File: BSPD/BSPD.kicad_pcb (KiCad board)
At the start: 2 copper layers, 76 x 56 mm, 32 parts, among them Q3 PMOS, U1 LM339DR, U10 641964-1, U2 SN74LVC1G08DBVR, U3 NE555DR, U4 SN74LVC3G14DCUR, U5 SN74AC32DR, U6 SN74LVC1G08DBVR, U7 641964-1, U8 R-78E5.0-0.5, U9 641964-1

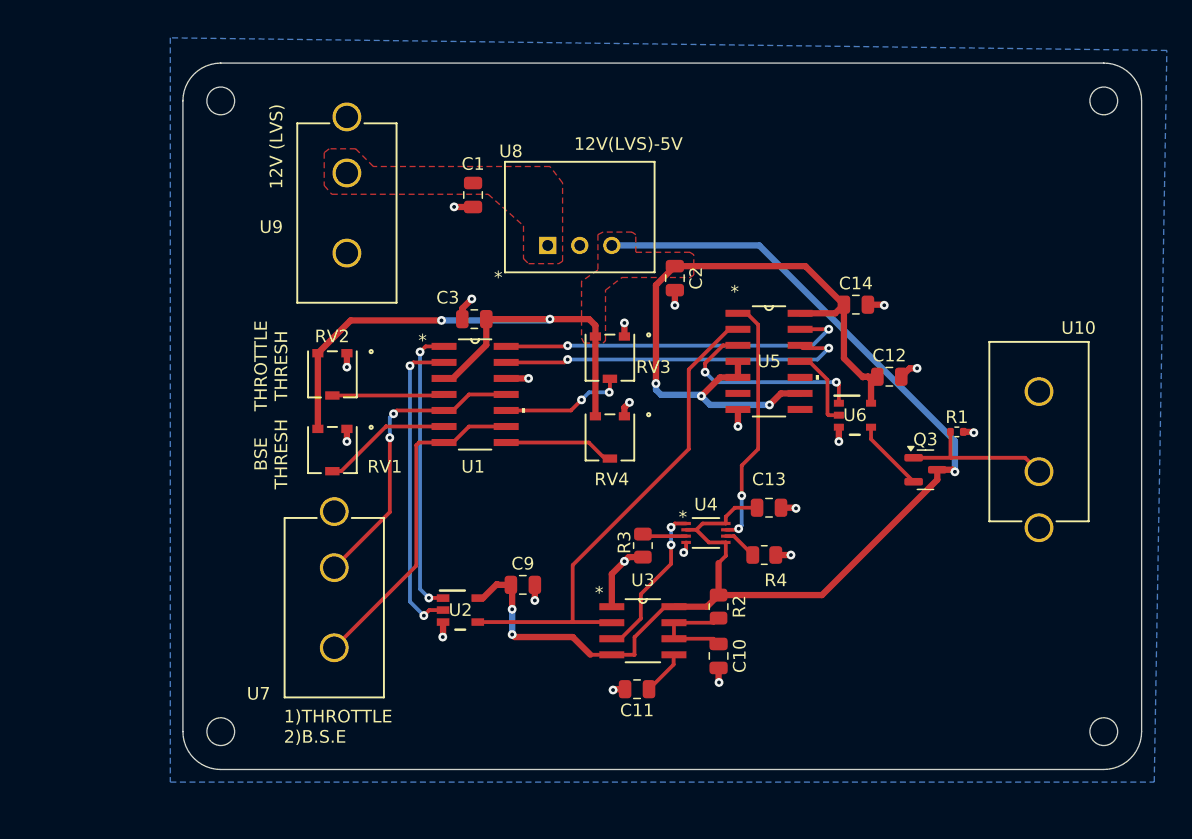
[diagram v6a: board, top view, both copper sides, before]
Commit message: JLC PCB BOM, placement redone to account for footprint changes, started re-routing
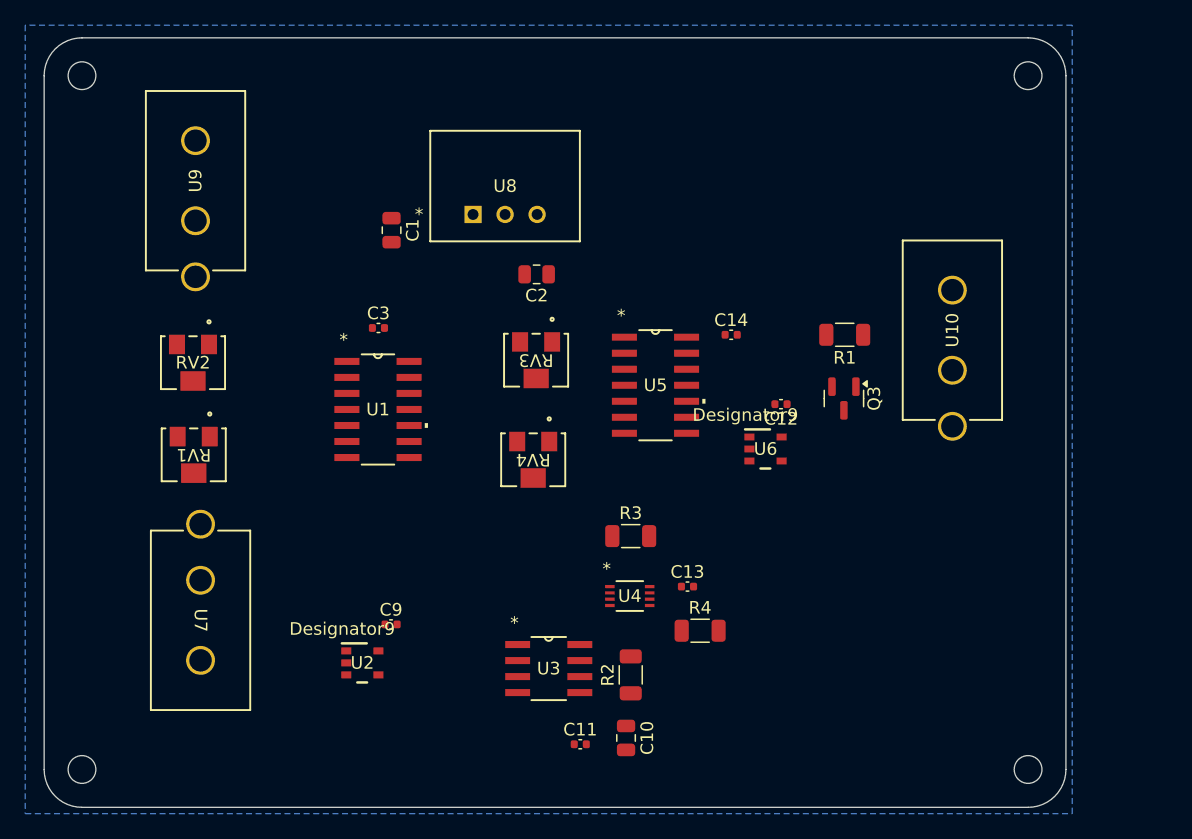
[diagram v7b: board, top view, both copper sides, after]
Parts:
- C11, C12, C13, C14, C3, C9: footprint Capacitor_SMD:C_0805_2012Metric -> Capacitor_SMD:C_0402_1005Metric
- R1: footprint Resistor_SMD:R_0402_1005Metric -> Resistor_SMD:R_1206_3216Metric
- R2, R3, R4: footprint Resistor_SMD:R_0805_2012Metric -> Resistor_SMD:R_1206_3216Metric
- RV1, RV2, RV3, RV4: footprint PVG3A103C01R00:RES_C01R00 -> 3224W-1-103E:POT_3224W
- U2: footprint SN74LVC1G08DBVR:DBV0005A_N -> SN74LVC1G08DBVR:DBV0005A_L
- moved U9 12.6 mm to (119.0, 101.5), turned to 90 degrees
- moved R1 11.8 mm to (170.5, 110.5), turned to 180 degrees
- moved H2 11.4 mm to (110.0, 145.0)
- moved H1 11.2 mm to (110.0, 90.0)
- moved RV2 11.1 mm to (118.8, 112.8)
- moved RV1 11.0 mm to (118.9, 120.1)
- moved C2 11.0 mm to (146.0, 105.8), turned to 180 degrees
- moved C9 10.9 mm to (134.5, 133.5)
- moved U7 10.6 mm to (119.4, 130.0)
- moved U10 10.6 mm to (179.0, 113.3)
- moved C14 10.2 mm to (161.5, 110.5)
- moved C10 9.80 mm to (153.1, 142.5)
- moved U5 9.20 mm to (155.5, 114.5)
- moved C13 8.99 mm to (158.0, 130.5)
- moved C12 8.86 mm to (165.4, 116.0), turned to 180 degrees
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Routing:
- net +5V: track 203.9 -> 0.00 mm, vias 8 -> 0
- net Net-(U2-Y): track 39.7 -> 0.00 mm
- net GND: track 30.5 -> 0.00 mm, vias 21 -> 0
- net 3OUT: track 28.4 -> 0.00 mm, vias 2 -> 0
- net 4OUT: track 28.4 -> 0.00 mm, vias 2 -> 0
- net BSE_IN: track 26.5 -> 0.00 mm
- net 2OUT: track 24.8 -> 0.00 mm, vias 2 -> 0
- net THROTTLE_IN: track 23.7 -> 0.00 mm, vias 2 -> 0
- net 1OUT: track 23.0 -> 0.00 mm, vias 2 -> 0
- net Net-(U4-1Y): track 19.8 -> 0.00 mm, vias 2 -> 0
- net Net-(U5-1Y): track 16.4 -> 0.00 mm, vias 2 -> 0
- net Net-(U3-OUT): track 12.5 -> 0.00 mm, vias 2 -> 0
- net BSPD_TO_FAULT: track 12.5 -> 0.00 mm
- net THRESH_BSE: track 10.3 -> 0.00 mm
- net 10%_THROTTLE: track 9.86 -> 0.00 mm, vias 2 -> 0
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- removed copper zone on F.Cu, net +12V
- removed copper zone on F.Cu, net +5V
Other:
- board size 76 x 56 mm -> 81 x 61 mm
- board text removed: "1)THROTTLE 2)B.S.E"
- board text removed: "12V (LVS)"
- board text removed: "12V(LVS)-5V"
- board text removed: "BSE THRESH"
- board text removed: "THROTTLE THRESH"

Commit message: Routing, final BOM
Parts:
- moved C11 4.50 mm to (149.5, 138.5), turned to 180 degrees
- moved R3 4.30 mm to (157.0, 124.0)
- moved R4 4.30 mm to (162.5, 131.5)
- moved U4 4.30 mm to (156.9, 128.8)
- moved U2 4.08 mm to (135.7, 134.5)
- moved C9 4.08 mm to (138.0, 131.4)
- moved C14 4.07 mm to (165.5, 110.5)
- moved U5 4.07 mm to (159.5, 114.5)
- moved U10 3.99 mm to (180.4, 117.1)
- moved C13 3.81 mm to (159.5, 127.0)
- moved Q3 3.46 mm to (172.9, 117.9)
- moved R1 3.46 mm to (173.0, 112.9)
- moved RV1 3.38 mm to (121.9, 121.6)
- moved U7 3.38 mm to (122.4, 131.6)
- moved U9 3.38 mm to (122.0, 103.1)
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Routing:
- net +5V: track 0.00 -> 142.9 mm, vias 0 -> 12
- net Net-(U2-Y): track 0.00 -> 38.1 mm, vias 0 -> 2
- net GND: track 0.00 -> 33.2 mm, vias 0 -> 22
- net 3OUT: track 0.00 -> 29.3 mm, vias 0 -> 2
- net 4OUT: track 0.00 -> 29.2 mm, vias 0 -> 2
- net 2OUT: track 0.00 -> 28.8 mm, vias 0 -> 2
- net BSE_IN: track 0.00 -> 27.0 mm
- net 1OUT: track 0.00 -> 25.1 mm, vias 0 -> 2
- net THROTTLE_IN: track 0.00 -> 24.6 mm, vias 0 -> 2
- net Net-(U4-1Y): track 0.00 -> 20.6 mm, vias 0 -> 2
- net Net-(U5-1Y): track 0.00 -> 17.7 mm, vias 0 -> 2
- net Net-(U3-OUT): track 0.00 -> 16.7 mm
- net 10%_THROTTLE: track 0.00 -> 13.6 mm
- net HARD_BREAK: track 0.00 -> 12.4 mm
- net THRESH_BSE: track 0.00 -> 11.9 mm
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- added copper zone on F.Cu, net +12V
- added copper zone on F.Cu, net +5V
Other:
- board text added: "1)THROTTLE 2)B.S.E."
- board text added: "12(LVS) TO 5V"
- board text added: "12V (LVS)"
- board text added: "B.S.E THRESH"
- board text added: "THROTTLE THRESH"
